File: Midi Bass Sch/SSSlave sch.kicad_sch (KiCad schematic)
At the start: 1 part

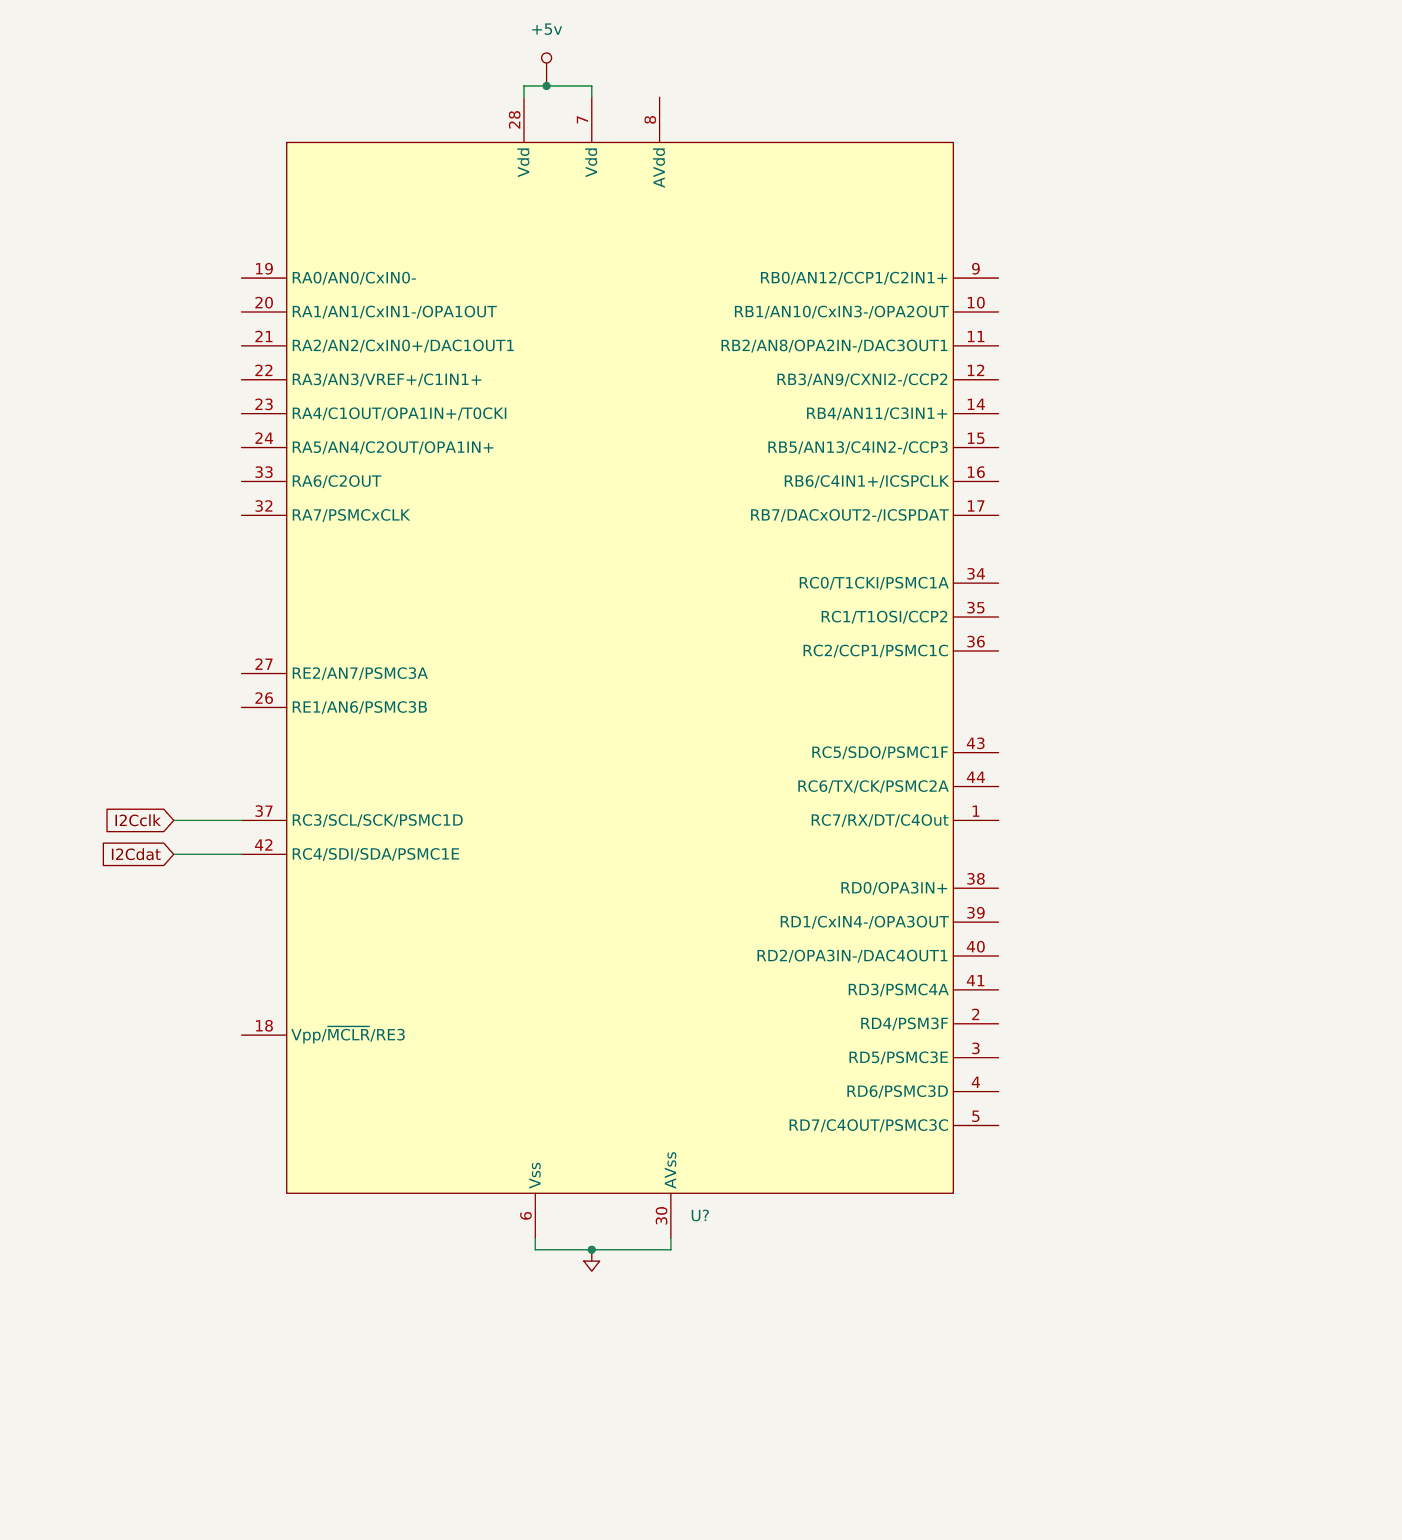
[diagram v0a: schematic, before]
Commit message: updated schematic to include solenoids for pluck slave
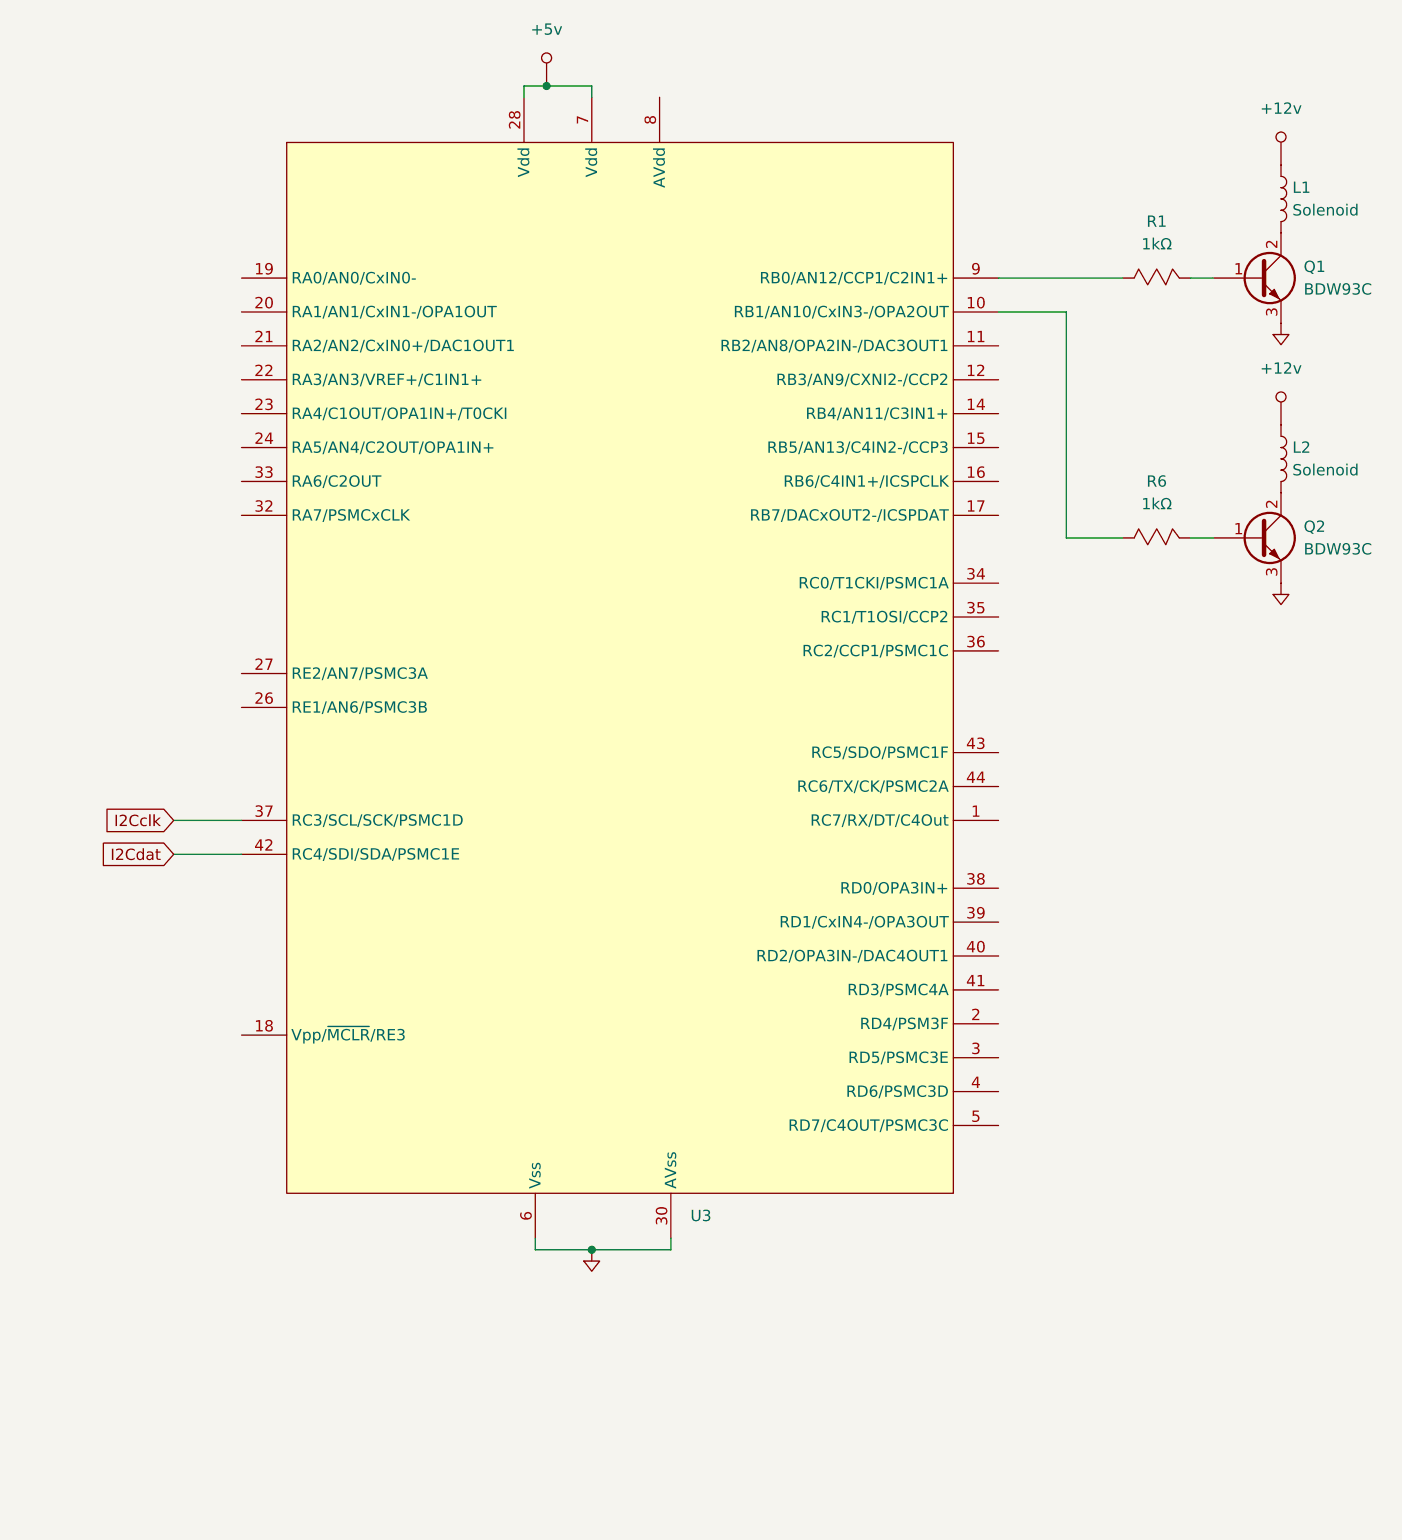
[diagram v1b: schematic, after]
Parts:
- added L1, L2: Solenoid, symbol Device:L
- added Q1, Q2: BDW93C, symbol Device:Q_NPN_BCE
- added R1, R6: 1kΩ, symbol Custom Symbols:Resistor_Mod
- gave numbers to parts that had none: 1
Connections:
- net GND: now also Q1.3 (E), Q2.3 (E)
- net at U3.10 (RB1/AN10/CxIN3-/OPA2OUT): now also R6.1
- net at U3.9 (RB0/AN12/CCP1/C2IN1+): now also R1.1
- new net: L1.2, Q1.2 (C)
- new net: Q1.1 (B), R1.2
- new net: L2.2, Q2.2 (C)
- new net: Q2.1 (B), R6.2
- new net +12v: L1.1, L2.1

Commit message: added startup clear to schematic
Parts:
- added C3: 10uF, symbol Owen's Symbols:Capacitor
- added D4: 4148, symbol Owen's Symbols:Diode
- added R8: 10kΩ, symbol Owen's Symbols:Resistor_Mod
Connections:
- net +5v: now also R8.2
- net GND: now also C3.2
- net at U3.18 (Vpp/~{MCLR}/RE3): now also D4.2
- new net: C3.1, D4.1, R8.1

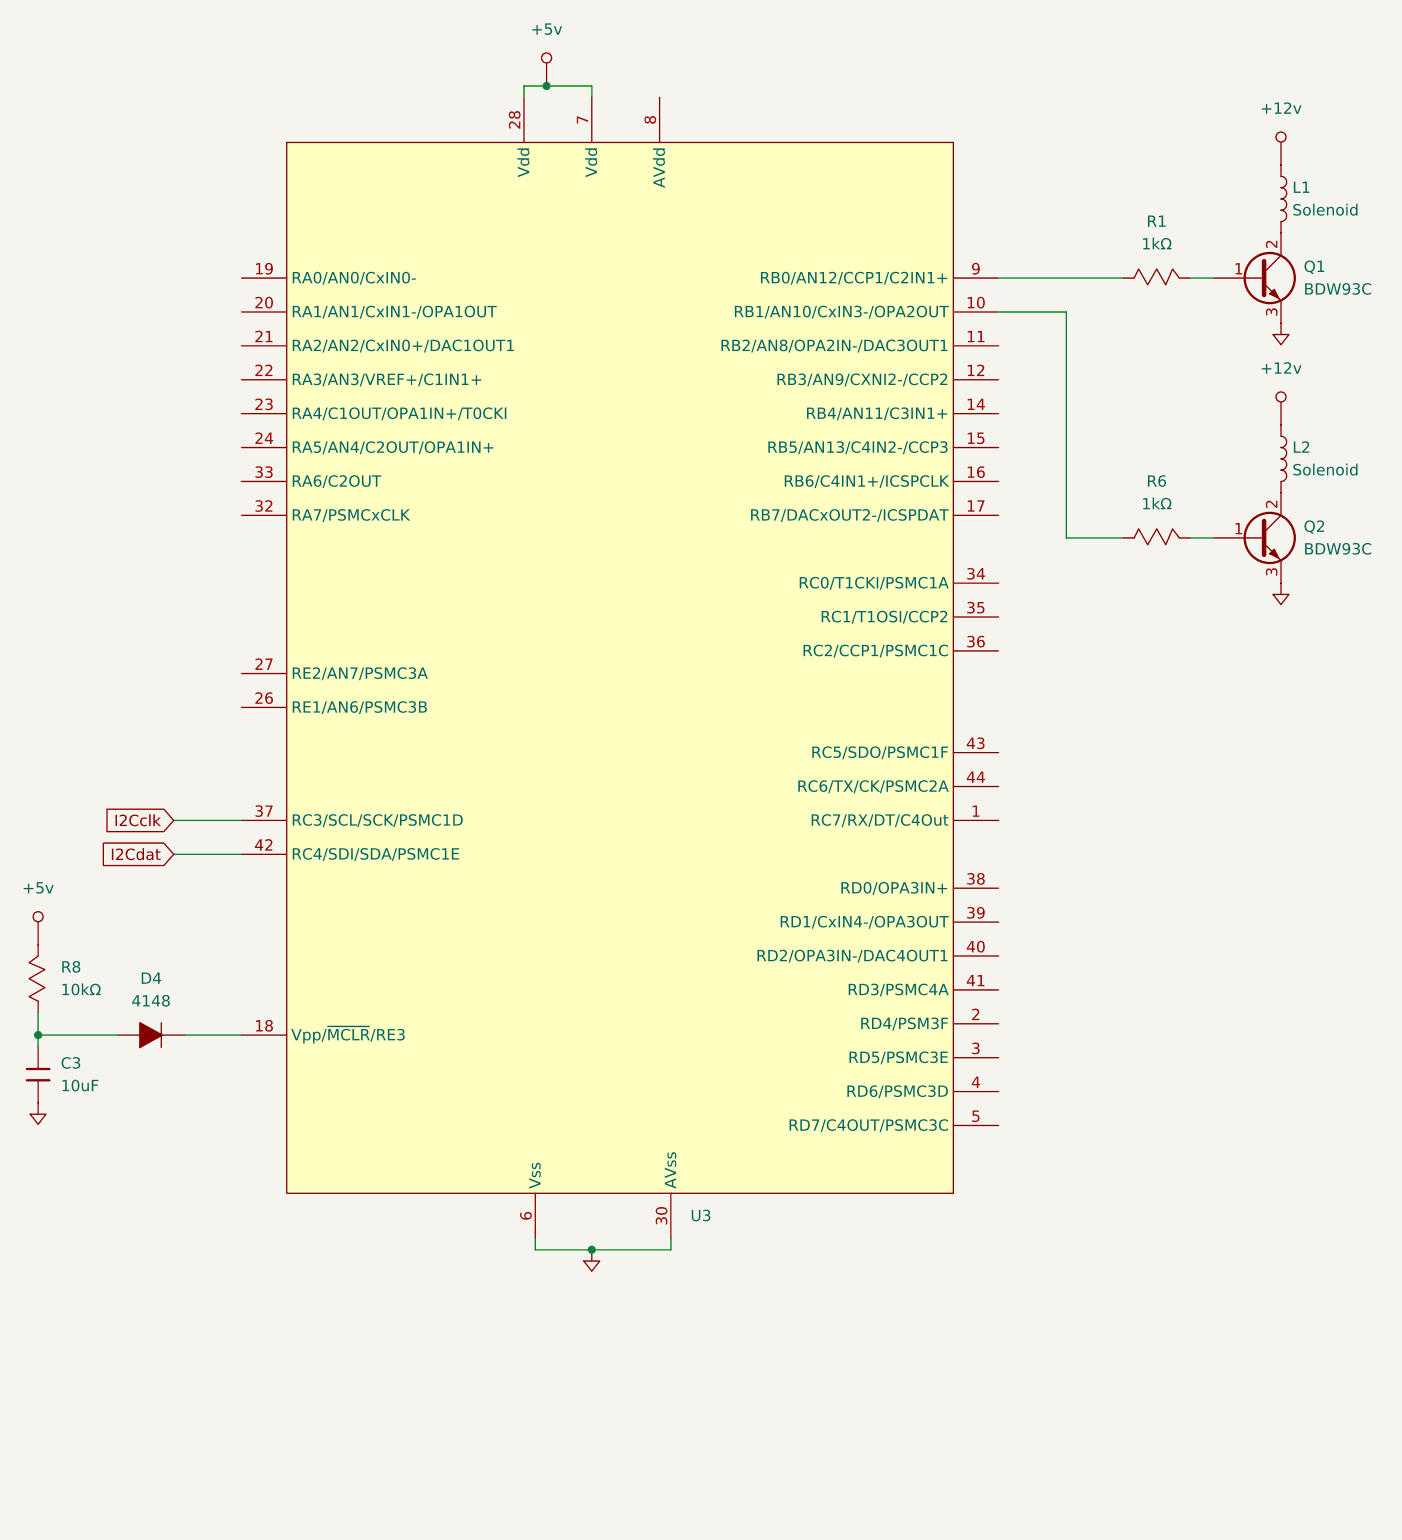
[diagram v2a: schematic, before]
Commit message: changed solenoid to a seperate sheet to include all plucking units
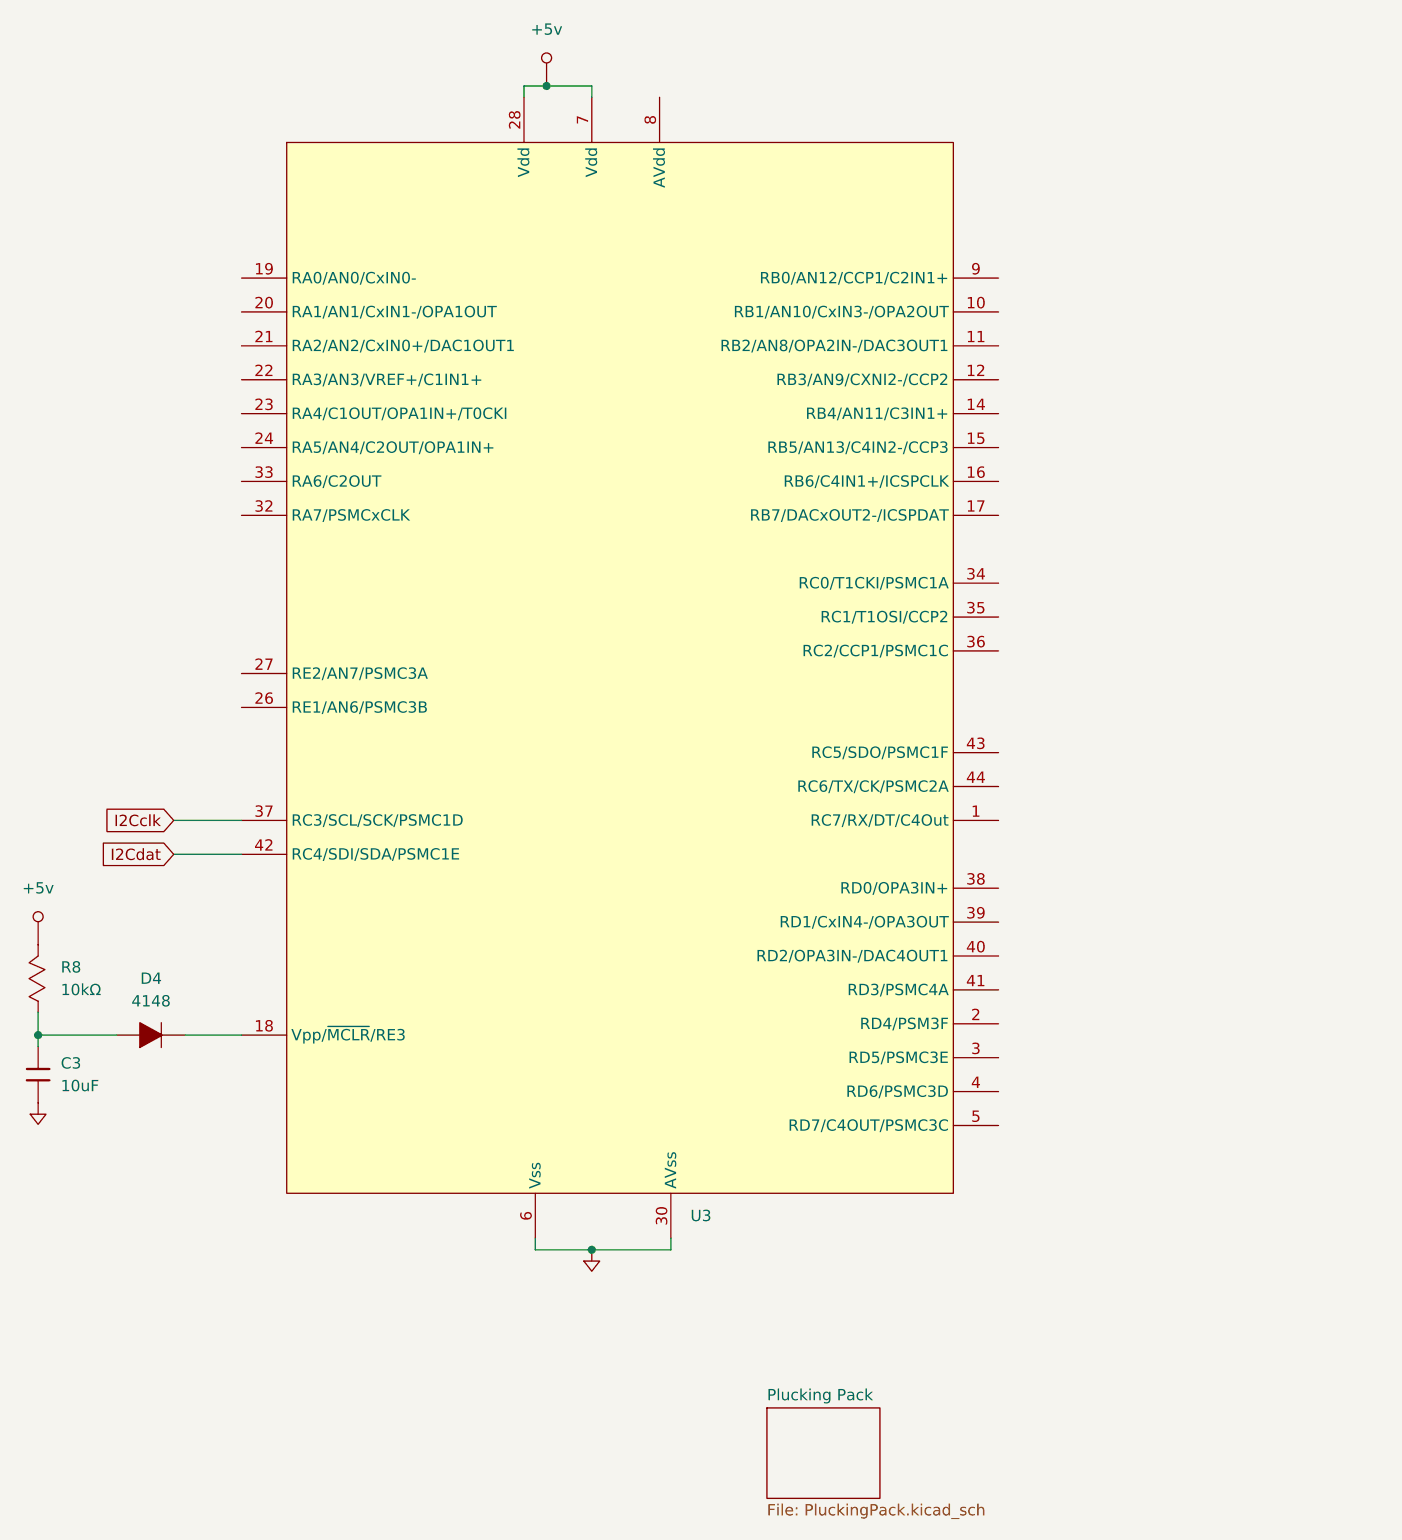
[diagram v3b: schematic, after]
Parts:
- removed L1, L2: Solenoid, symbol Device:L
- removed Q1, Q2: BDW93C, symbol Device:Q_NPN_BCE
- removed R1, R6: 1kΩ, symbol Custom Symbols:Resistor_Mod
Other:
- added sheet Plucking Pack (PluckingPack.kicad_sch)
